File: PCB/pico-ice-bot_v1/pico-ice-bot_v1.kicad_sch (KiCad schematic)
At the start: 1 part

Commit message: updated some files
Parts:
- added J1: Mot1, Connector_PinSocket_2.54mm:PinSocket_1x06_P2.54mm_Vertical, symbol Connector:Conn_01x06_Socket
- added J2: Mot2, Connector_PinSocket_2.54mm:PinSocket_1x06_P2.54mm_Vertical, symbol Connector:Conn_01x06_Socket
- added J3: Conn_01x04_Socket, Connector_PinHeader_2.54mm:PinHeader_1x04_P2.54mm_Vertical, symbol Connector:Conn_01x04_Socket
- added J4: PMOD, Connector_PinSocket_2.54mm:PinSocket_1x06_P2.54mm_Vertical, symbol Connector:Conn_01x06_Socket
- added R1, R2: KDV12FR180ET, Resistor_SMD:R_1206_3216Metric_Pad1.30x1.75mm_HandSolder, symbol Device:R_US
- added R3, R4, R5: R_US, Resistor_SMD:R_0603_1608Metric_Pad0.98x0.95mm_HandSolder, symbol Device:R_US
- added RN1: 742X083101JP, Resistor_SMD:R_Array_Concave_4x0603, symbol Device:R_Pack04
- added U2: DRV8411RTER, DRV8411:QFN50P300X300X80-17N-D, symbol DRV8411:DRV8411RTER
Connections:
- net +3.3V: now also J1.2 (Pin_2), J2.2 (Pin_2), J4.1 (Pin_1), R3.1
- net GND: now also J1.5 (Pin_5), J2.5 (Pin_5), J3.4 (Pin_4), J4.2 (Pin_2), R1.2, R2.2, R5.2, U2.11 (GND), U2.17 (PAD)
- net enc2_b: now reaches U1.10 (ICE38)
- net enc2_b: now also J2.4 (Pin_4)
- net mot_sleep: now reaches U1.11 (ICE42)
- net mot_sleep: now also U2.15 (NSLEEP)
- net mot_fault: now reaches U1.12 (ICE43)
- net mot_fault: now also R3.2, U2.6 (NFAULT)
- net mot1_a: now reaches U1.17 (ICE44)
- net mot1_a: now also U2.14 (AIN1)
- net mot1_b: now reaches U1.18 (ICE45)
- net mot1_b: now also U2.13 (AIN2)
- net mot2_b: now reaches U1.19 (ICE46)
- net mot2_b: now also U2.8 (BIN2)
- net mot2_a: now reaches U1.20 (ICE47)
- net mot2_a: now also U2.7 (BIN1)
- net at U1.21 (ICE48): now also RN1.8 (R1.2)
- net at U1.22 (ICE2): now also RN1.7 (R2.2)
- net at U1.23 (ICE3): now also RN1.6 (R3.2)
- net at U1.24 (ICE4): now also RN1.5 (R4.2)
- net us_trig: now reaches U1.5 (ICE28)
- net us_trig: now also J3.2 (Pin_2)
- net us_echo: now reaches U1.6 (ICE31)
- net us_echo: now also R4.2, R5.1
- net enc1_a: now reaches U1.7 (ICE32)
- net enc1_a: now also J1.3 (Pin_3)
- net enc1_b: now reaches U1.8 (ICE34)
- net enc1_b: now also J1.4 (Pin_4)
- net enc2_a: now reaches U1.9 (ICE36)
- net enc2_a: now also J2.3 (Pin_3)
- new net: R1.1, U2.1 (AISEN)
- new net: J3.3 (Pin_3), R4.1
- new net: R2.1, U2.4 (BISEN)
- new net +5V: J3.1 (Pin_1)
- new net ICE2: J4.4 (Pin_4), RN1.2 (R2.1)
- new net ICE3: J4.5 (Pin_5), RN1.3 (R3.1)
- new net ICE4: J4.6 (Pin_6), RN1.4 (R4.1)
- new net ICE48: J4.3 (Pin_3), RN1.1 (R1.1)
- new net Pmot1_a: J1.1 (Pin_1), U2.16 (AOUT1)
- new net Pmot1_b: J1.6 (Pin_6), U2.2 (AOUT2)
- new net Pmot2_a: J2.1 (Pin_1), U2.5 (BOUT1)
- new net Pmot2_b: J2.6 (Pin_6), U2.3 (BOUT2)
- new net VBUS: U2.10 (VM)
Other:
- moved on the sheet: U1

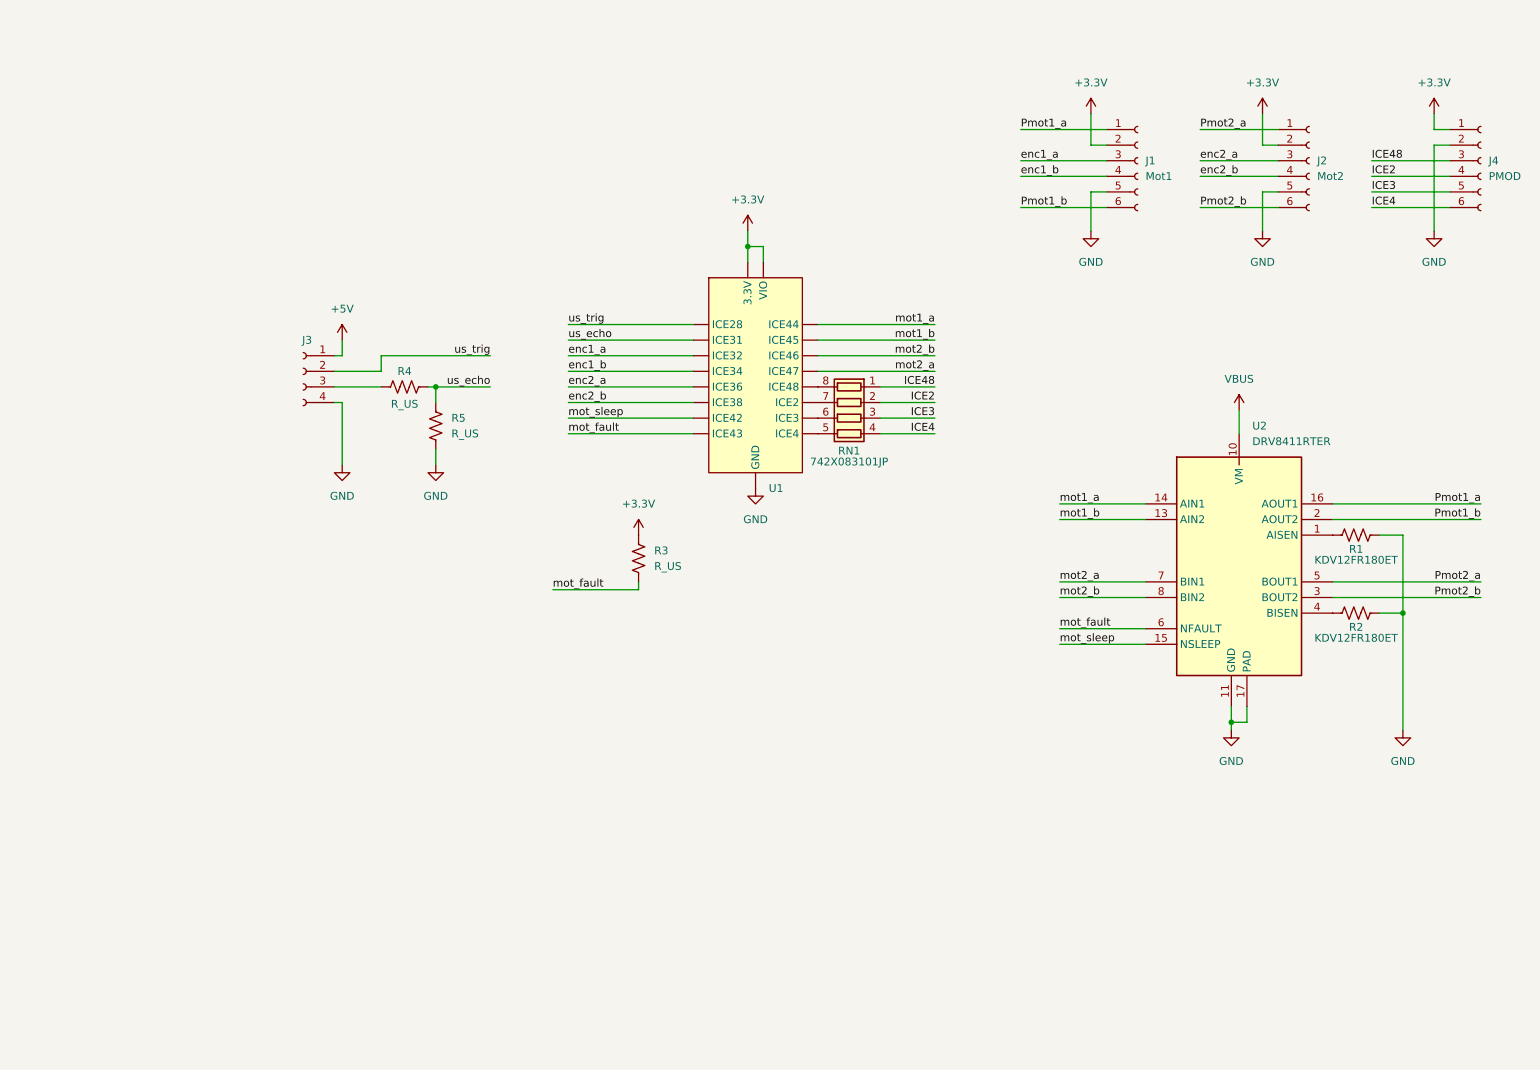
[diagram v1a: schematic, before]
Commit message: updated schematic and PCB Added batteries, power regulation
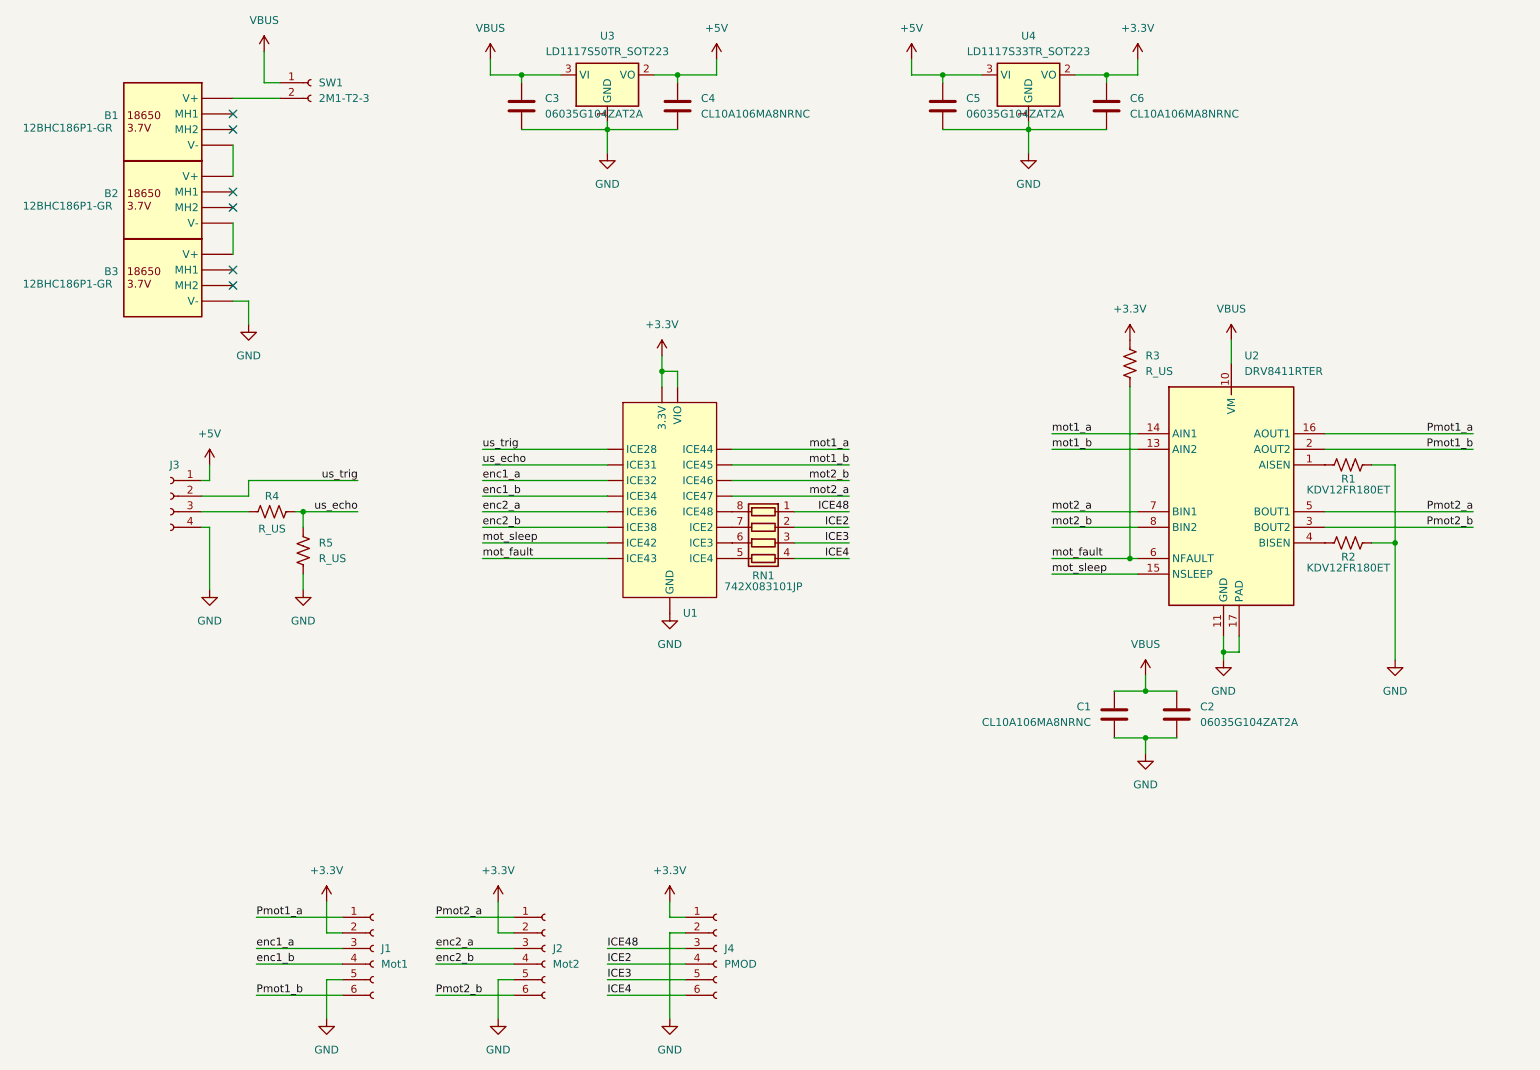
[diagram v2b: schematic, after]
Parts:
- added B1, B2, B3: 12BHC186P1-GR, Batteries:12BHC186P1GR, symbol Batteries:12BHC186P1-GR
- added C1, C4, C6: CL10A106MA8NRNC, Capacitor_SMD:C_0603_1608Metric_Pad1.08x0.95mm_HandSolder, symbol Device:C
- added C2, C3, C5: 06035G104ZAT2A, Capacitor_SMD:C_0603_1608Metric_Pad1.08x0.95mm_HandSolder, symbol Device:C
- added SW1: 2M1-T2-3, Connector_PinHeader_2.54mm:PinHeader_1x02_P2.54mm_Vertical, symbol Connector:Conn_01x02_Socket
- added U3: LD1117S50TR_SOT223, Package_TO_SOT_SMD:SOT-223-3_TabPin2, symbol Regulator_Linear:LD1117S50TR_SOT223
- added U4: LD1117S33TR_SOT223, Package_TO_SOT_SMD:SOT-223-3_TabPin2, symbol Regulator_Linear:LD1117S33TR_SOT223
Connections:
- net +3.3V: now also C6.1, U4.2 (VO)
- net +5V: now also C4.1, C5.1, U3.2 (VO), U4.3 (VI)
- net GND: now also B3.2 (V-), C1.2, C2.2, C3.2, C4.2, C5.2, C6.2, U3.1 (GND), U4.1 (GND)
- net VBUS: now also C1.1, C2.1, C3.1, SW1.1 (Pin_1), U3.3 (VI)
- new net: B1.1 (V+), SW1.2 (Pin_2)
- new net: B1.2 (V-), B2.1 (V+)
- new net: B2.2 (V-), B3.1 (V+)
- no-connect marks 0 -> 6
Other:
- moved on the sheet: J1, J2, J3, J4, R1, R2, R3, R4, R5, RN1, U1, U2

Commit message: update title block and adjust component positions in PCB and schematic files
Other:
- company: (none) -> Fred Corp.
- title: (none) -> Pice ICE Bot
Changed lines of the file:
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@@
 	(generator_version "9.0")
 	(paper "A4")
+	(title_block
+		(title "Pice ICE Bot")
+		(company "Fred Corp.")
+	)
 	(junction
 		(at 101.6 27.94)
